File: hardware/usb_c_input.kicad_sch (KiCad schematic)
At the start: 3 parts, among them J7 USB_C_Receptacle_USB2.0_16P, U10 TPD4EUSB30

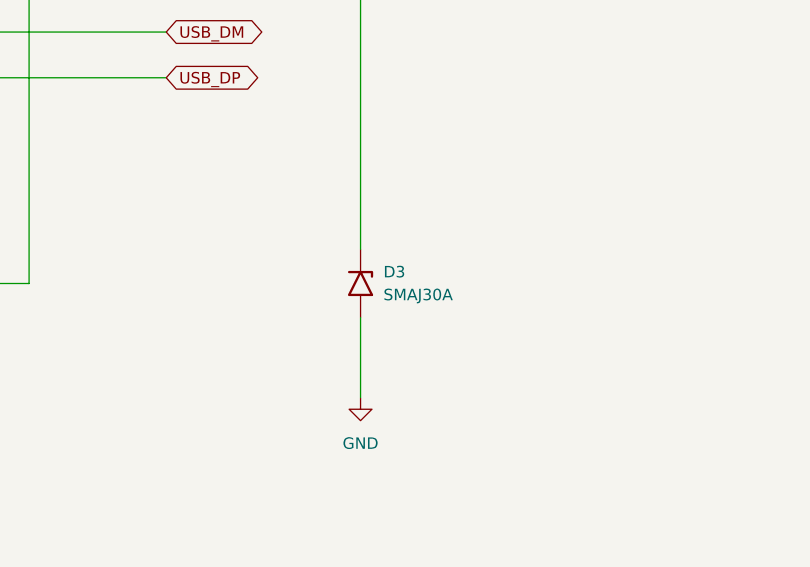
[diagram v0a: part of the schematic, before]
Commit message: usb_c_input: D3 SMAJ30A -> SMBJ30A (REV_C 3.1)
VBUS TVS'i 400 W SMA'dan 600 W SMB'ye yükseltildi.

Handoff dokümanı 3.1 #2'de D3'ü AQ3130E-01ETG (ESD diyotu) sanıyordu;
gerçekte D3 zaten USB_VBUS üzerinde tek yönlü 30 V TVS idi. ESD elemanı
ayrı: U10 = TPD4EUSB30. Bu yüzden "SMBJ30A ekle" maddesi mevcut TVS'in
yükseltilmesi olarak uygulandı.

ERC ve netlist değişmedi; yalnızca sembol, değer ve footprint.

Co-Authored-By: Claude Opus 5 <noreply@anthropic.com>
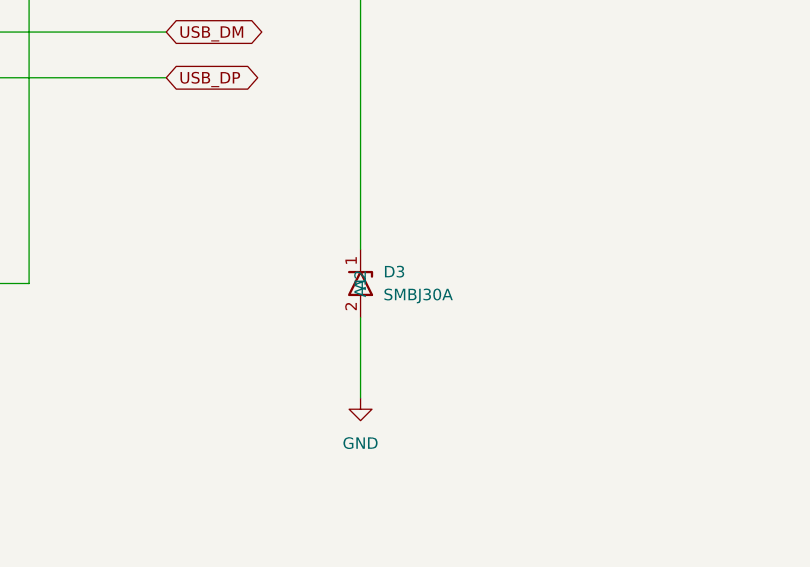
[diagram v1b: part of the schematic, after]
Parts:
- D3: value SMAJ30A -> SMBJ30A; footprint Diode_SMD:D_SMA -> Diode_SMD:D_SMB; symbol Diode:SMAJ30A -> Power_Path_Custom:SMBJ30A
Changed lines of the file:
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@@
 	)
 	(symbol
-		(lib_id "Diode:SMAJ30A")
+		(lib_id "Power_Path_Custom:SMBJ30A")
 		(at 210.82 118.11 270)
 		(unit 1)
@@
 			)
 		)
-		(property "Value" "SMAJ30A"
+		(property "Value" "SMBJ30A"
 			(at 213.36 119.3799 90)
 			(show_name no)
@@
 			)
 		)
-		(property "Footprint" "Diode_SMD:D_SMA"
+		(property "Footprint" "Diode_SMD:D_SMB"
 			(at 205.74 118.11 0)
 			(hide yes)
